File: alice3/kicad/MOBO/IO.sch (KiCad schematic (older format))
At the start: 18 parts, among them CON1 SD_Card, U10 LEVELCONVERTER, U11 LEVELCONVERTER, U6 MiniM4-D40, U7 DFROBOT_FTDI_BASIC, U8 LEVELCONVERTER, U9 LEVELCONVERTER

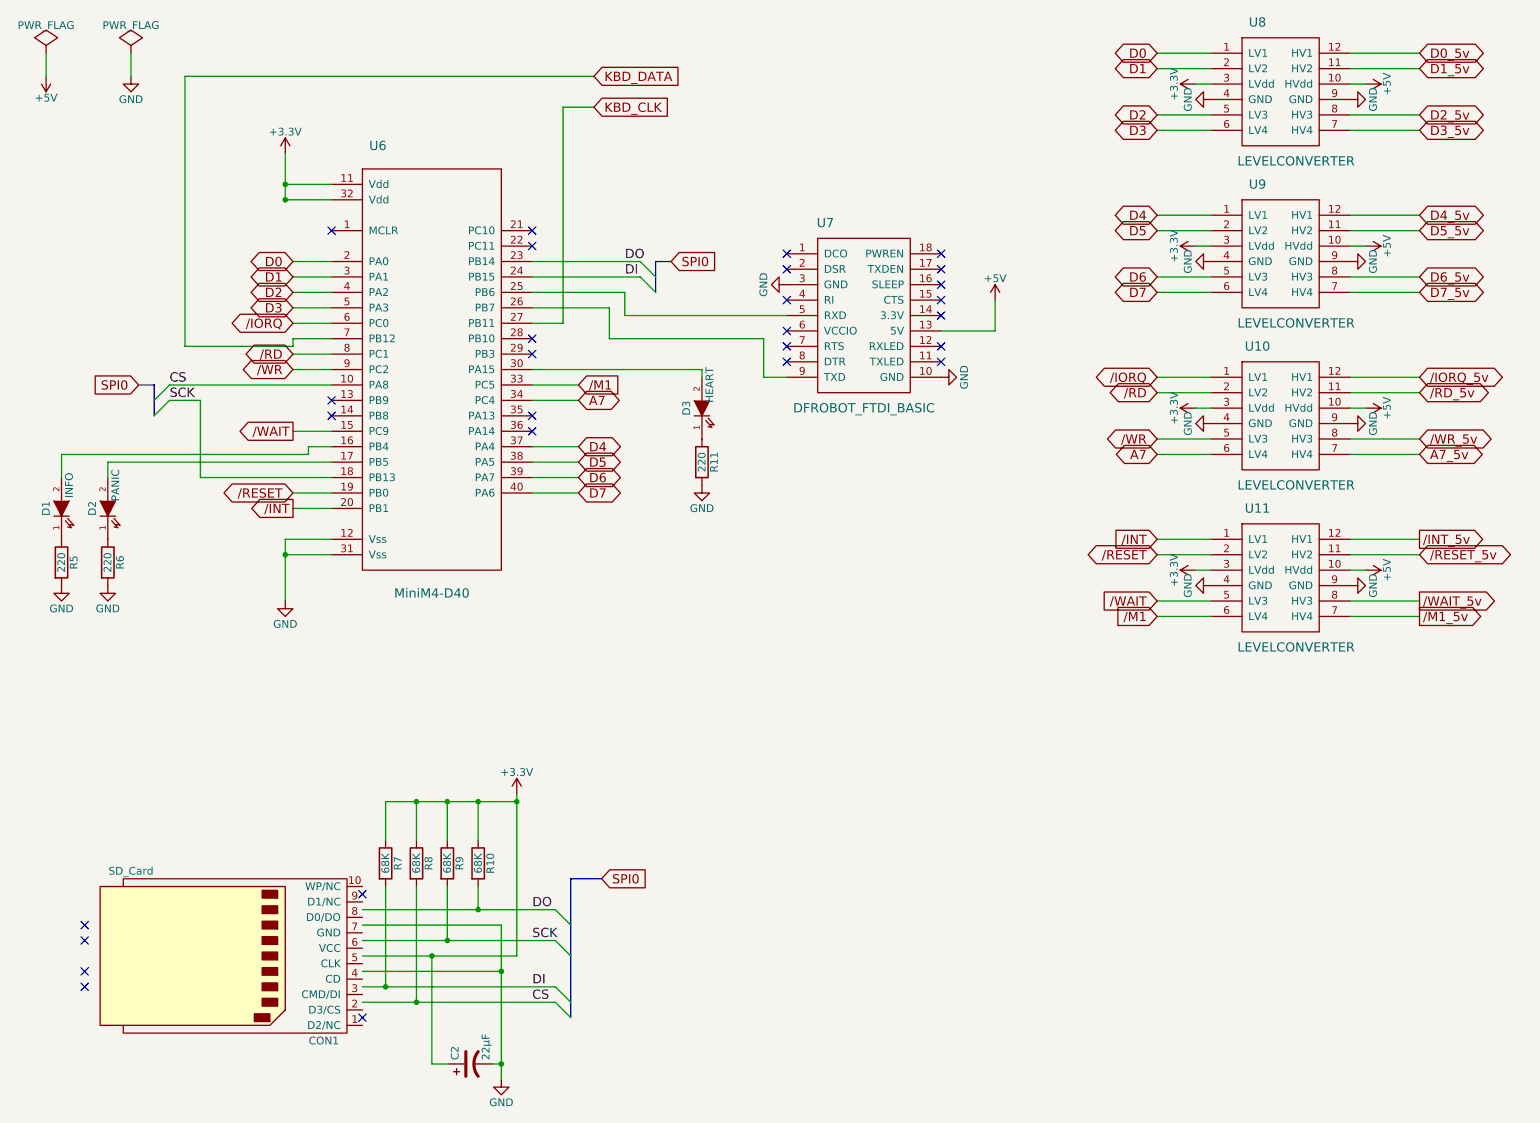
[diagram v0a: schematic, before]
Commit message: Add SRAM and EEPROM.
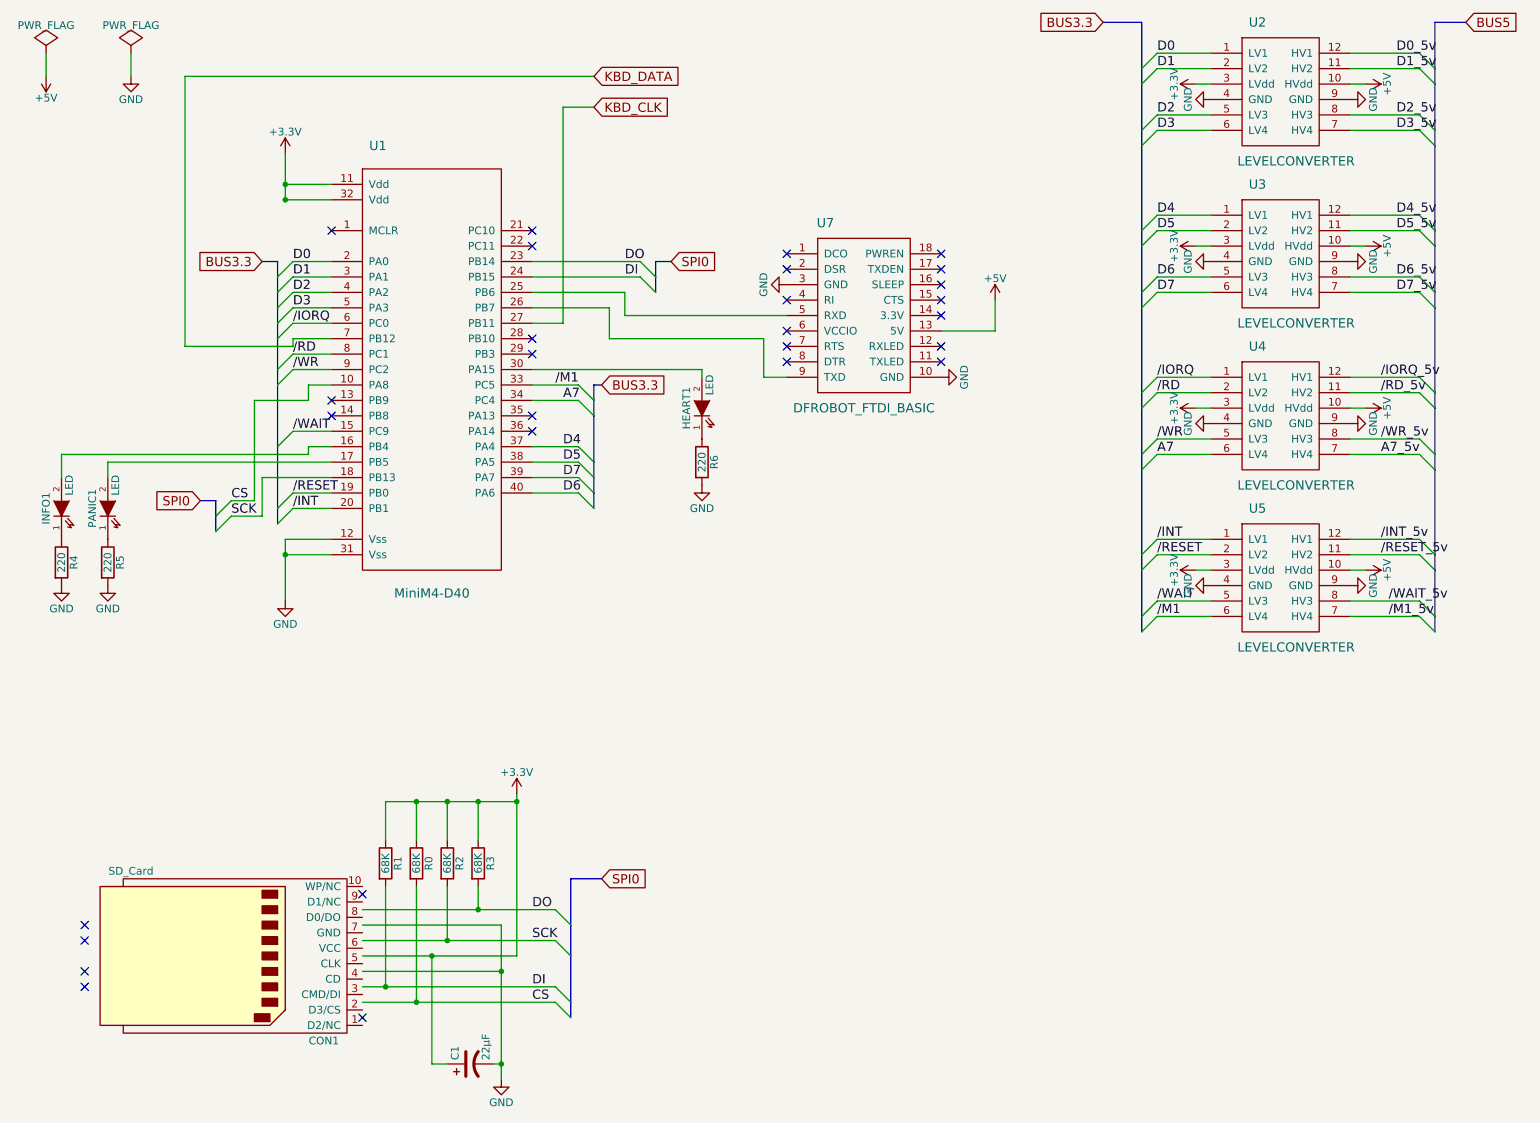
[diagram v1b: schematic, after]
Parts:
- HEART1: renamed from D3; value HEART -> LED
- INFO1: renamed from D1; value INFO -> LED
- PANIC1: renamed from D2; value PANIC -> LED
- renumbered C2 to C1, R8 to R0, R7 to R1, R9 to R2, R10 to R3, R5 to R4, R6 to R5, R11 to R6, U6 to U1, U8 to U2, U9 to U3, U10 to U4, U11 to U5
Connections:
- net labels added: BUS3.3, BUS5
- wire segments 117 -> 134
